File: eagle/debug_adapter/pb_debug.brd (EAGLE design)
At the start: 57.1 x 25.4 mm, 29 parts, among them J1 JTAG_14PIN_FULL, U1 MAX9910

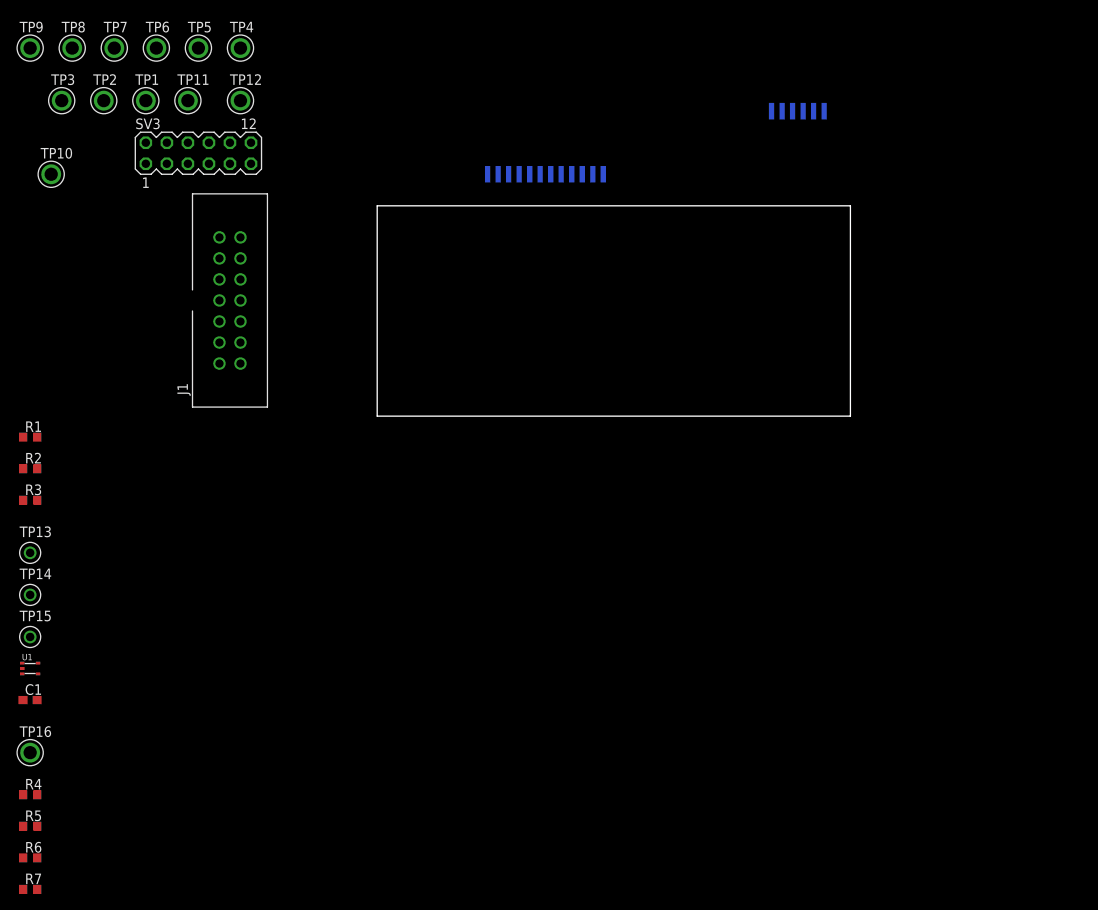
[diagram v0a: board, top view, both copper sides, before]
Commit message: moved some pins in debug adapter
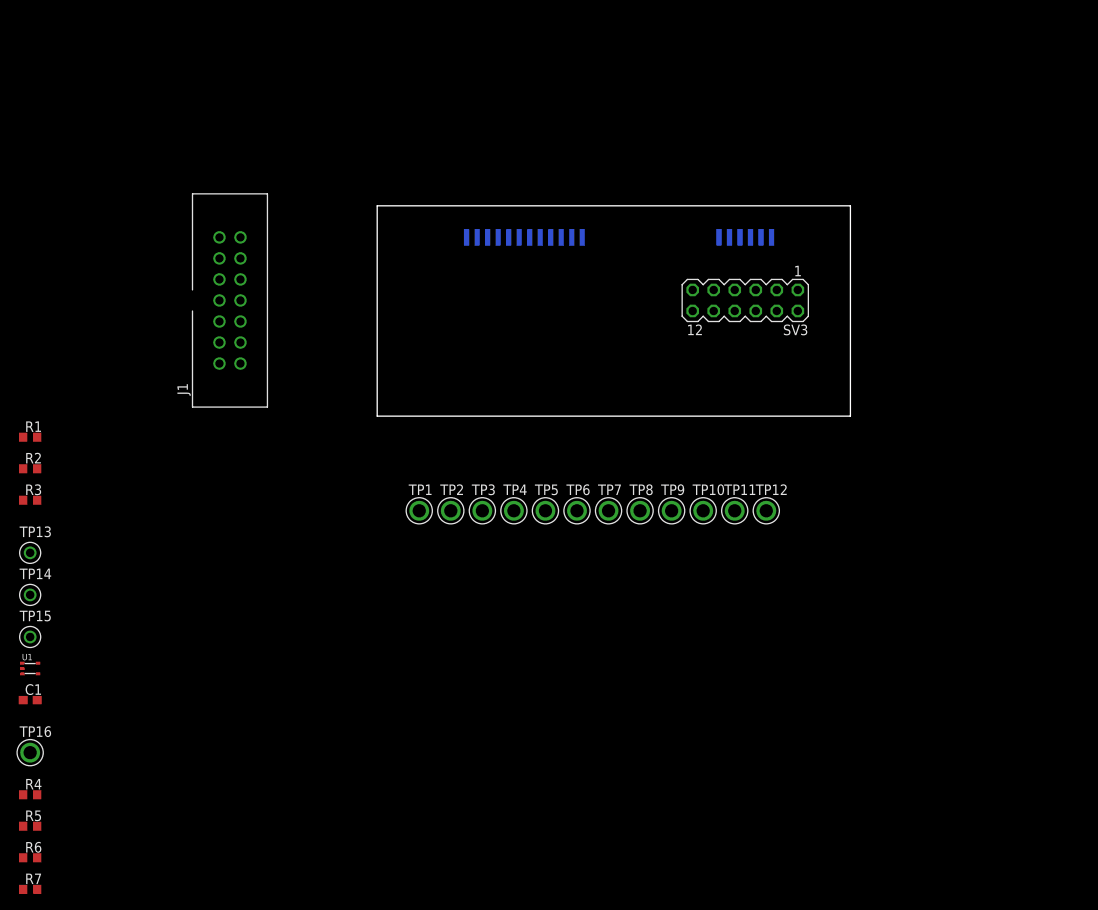
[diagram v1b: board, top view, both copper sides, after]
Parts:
- moved TP9 95.5 mm to (35.6, -11.4)
- moved TP10 88.6 mm to (39.4, -11.4)
- moved TP8 88.5 mm to (31.8, -11.4)
- moved TP11 82.5 mm to (43.2, -11.4)
- moved TP7 81.8 mm to (27.9, -11.4)
- moved TP12 80.5 mm to (47.0, -11.4)
- moved TP6 75.5 mm to (24.1, -11.4)
- moved TP3 70.9 mm to (12.7, -11.4)
- moved TP5 69.9 mm to (20.3, -11.4)
- moved SV3 68.4 mm to (44.5, 14.0), turned to 180 degrees
- moved TP4 64.9 mm to (16.5, -11.4)
- moved TP2 64.9 mm to (8.89, -11.4)
- moved TP1 59.5 mm to (5.08, -11.4)
- moved SV1 16.5 mm to (44.5, 21.6)
- moved SV2 8.03 mm to (17.8, 21.6)
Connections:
- net !RST!: now also SV3.4; no longer SV3.3
- net N$14: now also SV3.9; no longer SV3.10
- net N$15: now also SV3.7; no longer SV3.8
- net N$16: now also SV3.5; no longer SV3.6
- net N$17: now also SV3.3; no longer SV3.4
- net N$18: now also SV3.1; no longer SV3.2
- net N$7: now also SV3.11; no longer SV3.12
- net TCK: now also SV3.6; no longer SV3.5
- net TDI: now also SV3.10; no longer SV3.9
- net TDO: now also SV3.12; no longer SV3.11
- net TEST: now also SV3.2; no longer SV3.1
- net TMS: now also SV3.8; no longer SV3.7

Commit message: edits to pb_debug board
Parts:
- moved R7 91.8 mm to (14.6, 15.2), turned to 180 degrees
- moved R6 89.8 mm to (14.6, 16.5), turned to 180 degrees
- moved J1 88.1 mm to (69.8, 5.08), turned to 90 degrees
- moved R5 86.8 mm to (8.26, 21.3), turned to 180 degrees
- moved R4 80.4 mm to (5.71, 19.1), turned to 270 degrees
- moved TP15 77.2 mm to (23.5, 14.3)
- moved TP14 72.1 mm to (20.6, 14.3)
- moved C1 71.8 mm to (8.26, 17.1), turned to 180 degrees
- moved R3 71.0 mm to (23.5, 17.5), turned to 270 degrees
- moved U1 70.0 mm to (7.62, 19.1), turned to 270 degrees
- moved TP16 69.3 mm to (3.81, 11.4)
- moved R2 66.9 mm to (20.6, 17.5), turned to 270 degrees
- moved TP13 66.6 mm to (17.1, 14.3)
- moved R1 62.4 mm to (17.1, 17.5), turned to 270 degrees
- moved SV1 25.4 mm to (69.8, 21.6)
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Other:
- board size 57.1 x 25.4 mm -> 82.5 x 25.4 mm

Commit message: finished pb debug board
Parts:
- added J2: MA02-1STR, con-lstb:MA02-1
- added LED1: (no value), SparkFun-LED:LED-0603
- added Q1: 2N7002, nav:SC-70-3
- added R8: (no value), rcl:R0603
- added R9: 240, rcl:R0603
- added TP17: TP_STD, skyspecs:TP
- moved R2 3.81 mm to (24.4, 17.5)
- moved SV2 3.81 mm to (27.9, 21.6)
- moved TP10 3.81 mm to (45.7, 11.4)
- moved TP11 3.81 mm to (49.5, 3.81)
- moved TP12 3.81 mm to (53.3, 11.4)
- moved TP14 3.81 mm to (24.4, 14.3)
- moved TP5 3.81 mm to (26.7, 3.81)
- moved TP8 3.81 mm to (38.1, 11.4)
- moved R4 3.81 mm to (9.53, 19.1)
- moved TP2 3.81 mm to (15.2, 11.4)
- moved TP3 3.81 mm to (19.1, 3.81)
- moved TP16 3.81 mm to (7.62, 11.4)
- moved TP1 3.81 mm to (11.4, 3.81)
- moved U1 3.81 mm to (11.4, 19.1)
- moved C1 3.81 mm to (12.1, 17.1)
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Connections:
- new net LED: Q1.P1, R8.2, TP17.P$1
- new net N$22: LED1.C, Q1.P3
- new net N$23: LED1.A, R9.1
- new net N$24: J2.2, R9.2
- net +3V3: now also J2.1
- net GND: now also Q1.P2
- net N$10: now also R8.1
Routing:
- net +3V3: track 0.00 -> 72.9 mm
- net N$12: track 0.00 -> 30.3 mm
- net N$10: track 0.00 -> 25.9 mm, vias 0 -> 1
- net N$13: track 0.00 -> 24.5 mm
- net N$1: track 0.00 -> 23.1 mm, vias 0 -> 1
- net N$5: track 0.00 -> 20.8 mm, vias 0 -> 1
- net N$8: track 0.00 -> 20.1 mm
- net N$11: track 0.00 -> 20.1 mm
- net N$3: track 0.00 -> 19.6 mm
- net N$22: track 0.00 -> 18.3 mm
- net N$9: track 0.00 -> 13.6 mm
- net N$2: track 0.00 -> 13.1 mm
- net N$6: track 0.00 -> 12.8 mm, vias 0 -> 1
- net TEST: track 0.00 -> 11.2 mm
- net N$4: track 0.00 -> 10.9 mm
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- added copper zone on layer 1, net GND
- added copper zone on layer 16, net GND
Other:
- board size 82.5 x 25.4 mm -> 83.8 x 25.4 mm
- board text added: "6.26.15"
- board text added: "LED"
- board text added: "PowerBlade Pitch Adapter"
- board text added: "S.DEBRUIN"
- board text added: "v1.0"
